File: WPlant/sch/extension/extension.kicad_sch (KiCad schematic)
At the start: 37 parts, among them J1 PROG/SWD, J2 HumSnc, J3 HumSnc, J4 HumSnc, J5 HumSnc, J6 Input, J7 Output, J8 LeakDetect, J9 Valves, Q1 FDS9926A, Q2 FDS9926A, U1 PY32F003F18P6TU, U2 74HC594, U3 4052, U4 AIP485BSA8.TB, U5 AIP485BSA8.TB, U6 AP2204R-5.0

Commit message: Extension sch update
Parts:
- U3: value 4052 -> 74HC4052
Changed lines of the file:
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@@
 			)
 		)
-		(property "Value" "4052"
+		(property "Value" "74HC4052"
 			(at 230.7941 99.06 0)
 			(effects

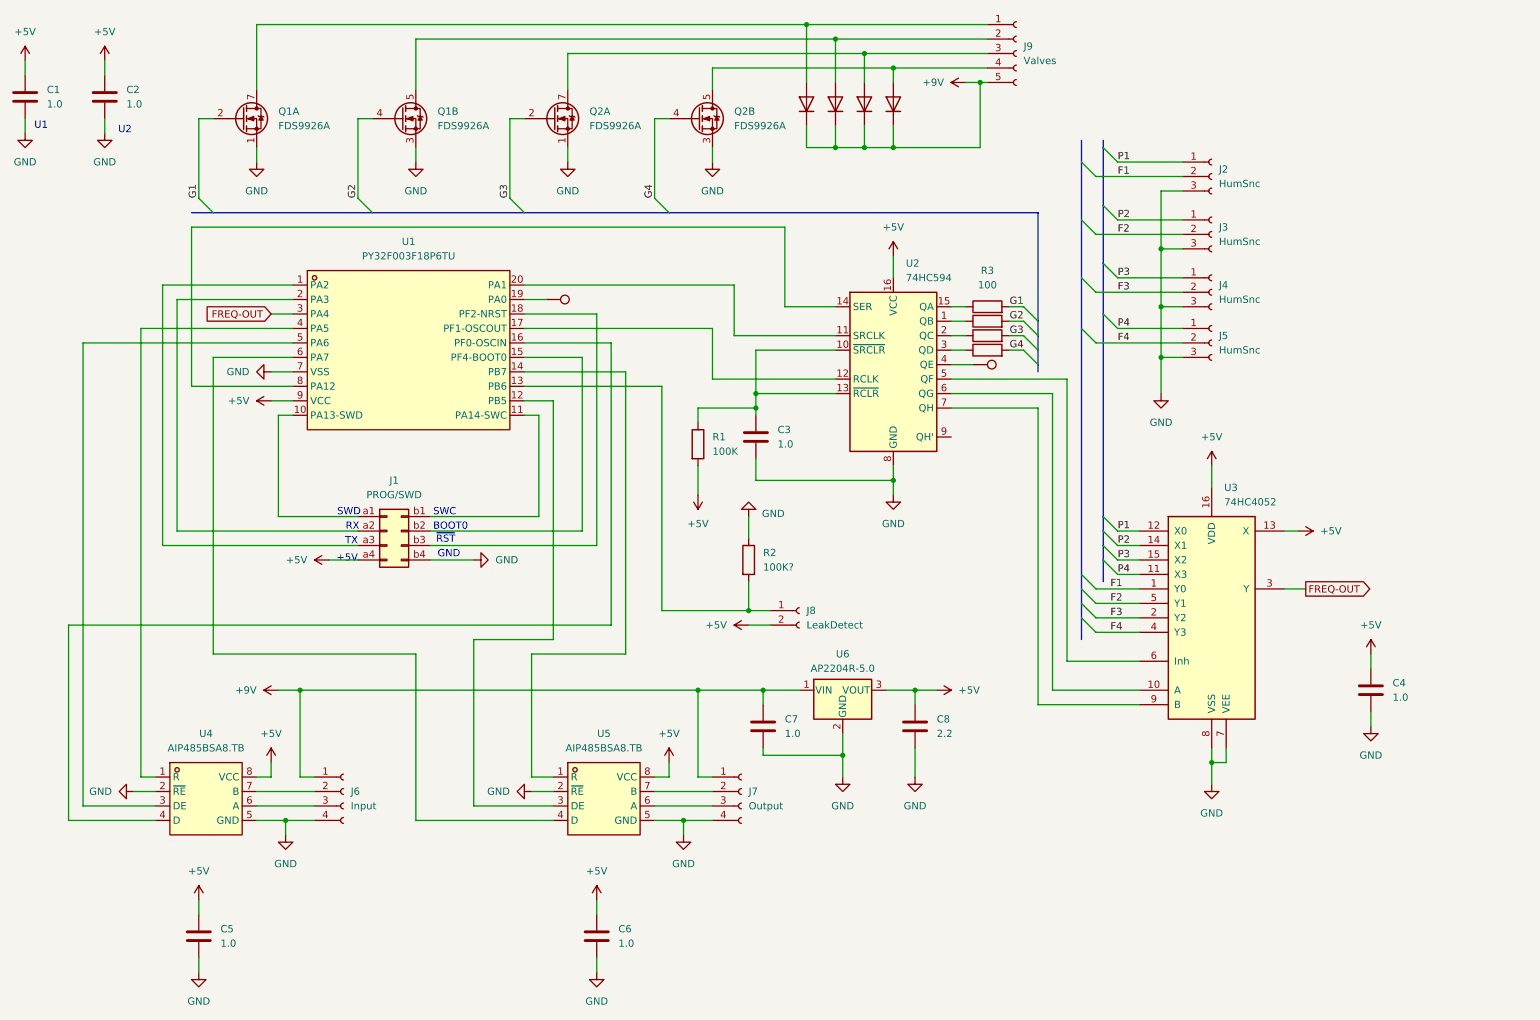
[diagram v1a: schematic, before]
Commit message: Updated Generic WP schematic
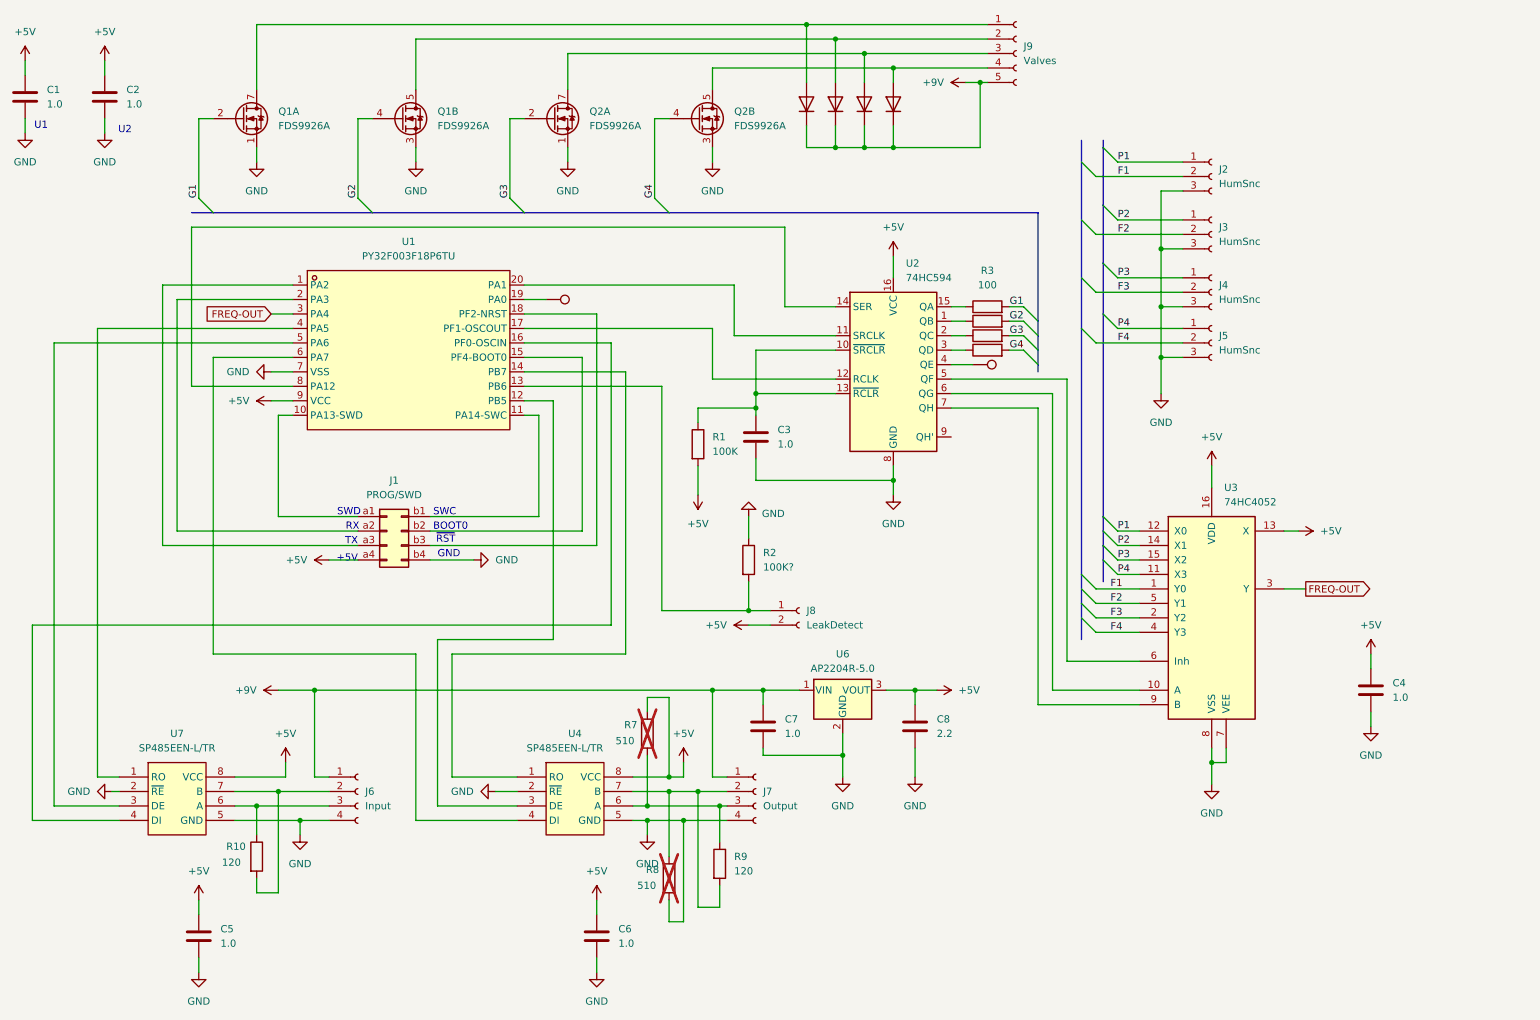
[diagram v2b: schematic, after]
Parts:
- removed U4, U5: AIP485BSA8.TB, easyeda2kicad:SOP-8_L4.9-W3.9-P1.27-LS6.0-BL, symbol EasyEDA:AIP485BSA8.TB
- added R10, R9: 120, symbol Device:R
- added R7, R8: 510, symbol Device:R
- added U4, U7: SP485EEN-L/TR, easyeda2kicad:SOIC-8_L5.0-W4.0-P1.27-LS6.0-BL, symbol EasyEDA:SP485EEN-L_TR
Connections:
- net +5V: now also R7.1, U4.8 (VCC), U7.8 (VCC)
- net GND: now also R8.2, U4.2 (~{RE}), U4.5 (GND), U7.2 (~{RE}), U7.5 (GND)
- net at J7.2 (Pin_2): now also R8.1, R9.2, U4.7 (B)
- net at J7.3 (Pin_3): now also R7.2, R9.1, U4.6 (A)
- net at U1.12 (PB5): now also U4.3 (DE)
- net at U1.14 (PB7): now also U4.1 (RO)
- net at U1.16 (PF0-OSCIN): now also U7.4 (DI)
- net at U1.4 (PA5): now also U7.1 (RO)
- net at U1.5 (PA6): now also U7.3 (DE)
- net at U1.6 (PA7): now also U4.4 (DI)
- net at J6.3 (Pin_3): now also R10.1, U7.6 (A)
- net at J6.2 (Pin_2): now also R10.2, U7.7 (B)
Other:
- moved on the sheet: J6, J7

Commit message: PCB for Extension block (of WP) ready
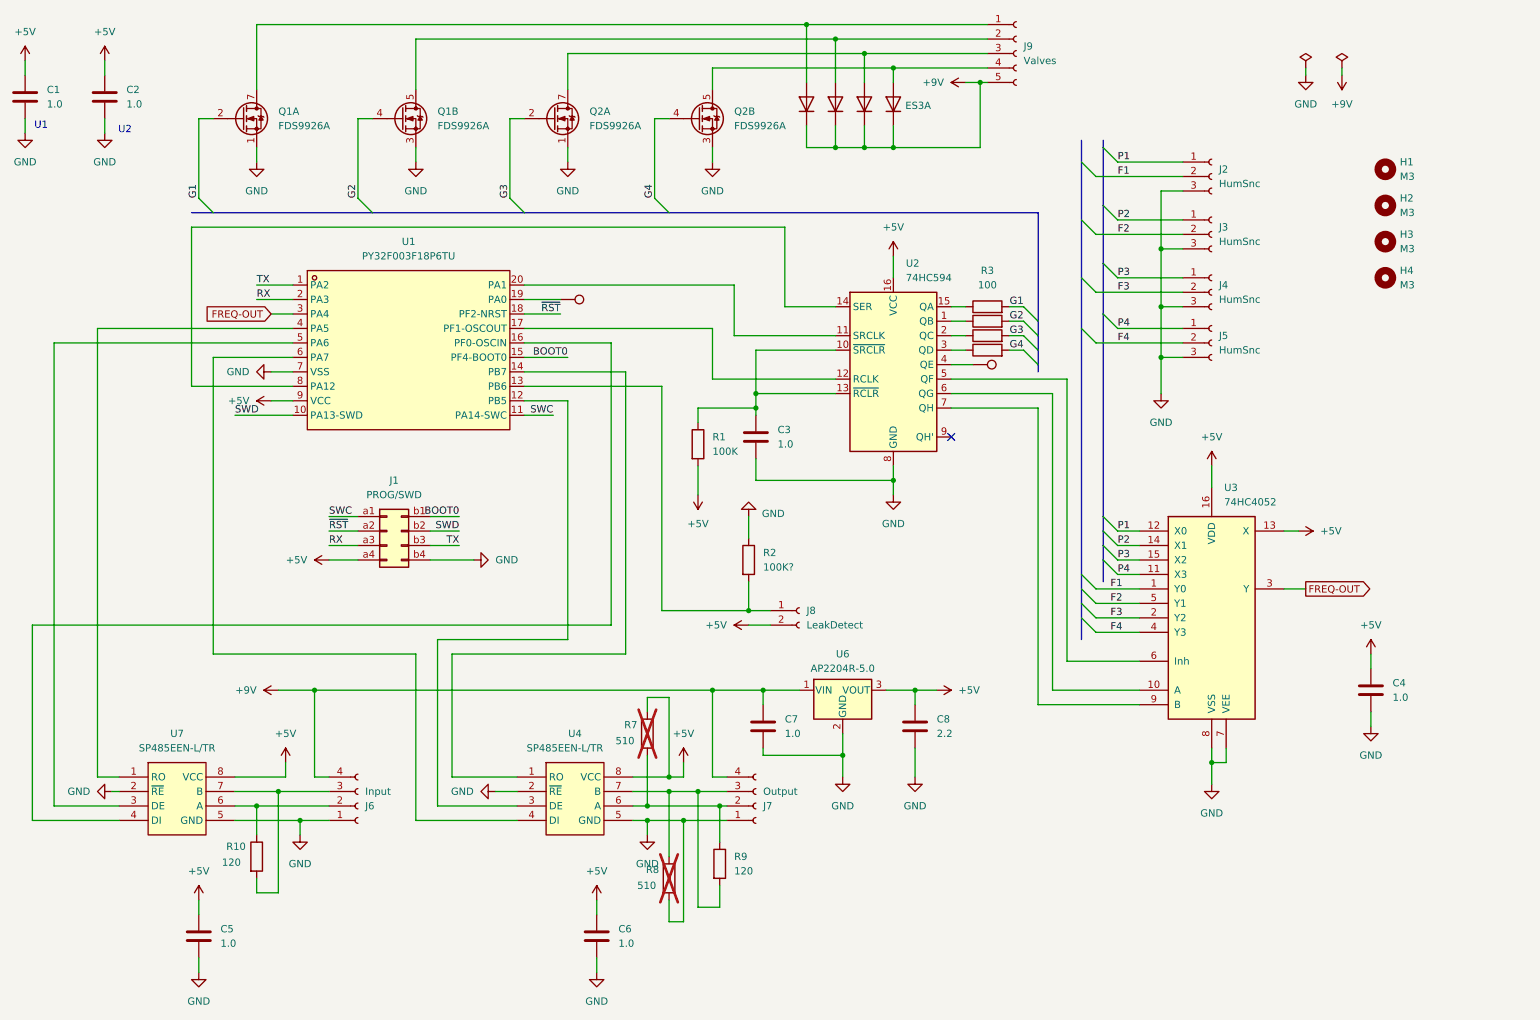
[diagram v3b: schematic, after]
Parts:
- added H1, H2, H3, H4: M3, MountingHole:MountingHole_3.2mm_M3, symbol Mechanical:MountingHole
- C1, C2, C3, C4, C5, C6, C7, C8: footprint (none) -> Capacitor_SMD:C_0603_1608Metric_Pad1.08x0.95mm_HandSolder
- D1, D2, D3, D4: value D -> ES3A; footprint (none) -> Diode_SMD:D_SMC
- J1: footprint (none) -> Connector_PinHeader_2.54mm:PinHeader_2x04_P2.54mm_Vertical
- J2, J3, J4, J5: footprint (none) -> easyeda2kicad:CONN-TH_DB301R-3.5-3P-GN-S
- J6, J7: footprint (none) -> local:CONN-TH_DB301R-3.5-4P-GN-S
- J8: footprint (none) -> Connector_JST:JST_XH_B2B-XH-A_1x02_P2.50mm_Vertical
- J9: footprint (none) -> Connector_JST:JST_XH_B5B-XH-A_1x05_P2.50mm_Vertical
- R1, R10, R2, R3, R4, R5, R6, R7, R8, R9: footprint (none) -> Resistor_SMD:R_0603_1608Metric_Pad0.98x0.95mm_HandSolder
- TP1, TP2: footprint (none) -> TestPoint:TestPoint_Pad_1.0x1.0mm
- U2: footprint (none) -> easyeda2kicad:SOIC-16_L9.9-W3.9-P1.27-LS6.0-BL
- U3: footprint (none) -> easyeda2kicad:SOP-16_L10.0-W3.9-P1.27-LS6.0-BL
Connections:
- net +9V: now also J6.4 (Pin_4), J7.4 (Pin_4); no longer J6.1 (Pin_1), J7.1 (Pin_1)
- net GND: now also J6.1 (Pin_1), J7.1 (Pin_1); no longer J6.4 (Pin_4), J7.4 (Pin_4)
- net SWC: now reaches J1.a1 (Pin_a1)
- net SWC: now also U1.11 (PA14-SWC); no longer U1.10 (PA13-SWD)
- net RX: now reaches U1.2 (PA3)
- net RX: now also J1.a3 (Pin_a3); no longer J1.a2 (Pin_a2)
- net TX: now reaches U1.1 (PA2)
- net TX: now also J1.b3 (Pin_b3); no longer J1.a3 (Pin_a3)
- net BOOT0: now reaches J1.b1 (Pin_b1)
- net BOOT0: now also U1.15 (PF4-BOOT0); no longer U1.11 (PA14-SWC)
- net SWD: now reaches J1.b2 (Pin_b2)
- net SWD: now also U1.10 (PA13-SWD); no longer U1.15 (PF4-BOOT0)
- net ~{RST}: now reaches U1.18 (PF2-NRST)
- net ~{RST}: now also J1.a2 (Pin_a2); no longer J1.b3 (Pin_b3)
- net at R8.1, R9.2, U4.7 (B): now also J7.3 (Pin_3); no longer J7.2 (Pin_2)
- net at R7.2, R9.1, U4.6 (A): now also J7.2 (Pin_2); no longer J7.3 (Pin_3)
- net at R10.1, U7.6 (A): now also J6.2 (Pin_2); no longer J6.3 (Pin_3)
- net at R10.2, U7.7 (B): now also J6.3 (Pin_3); no longer J6.2 (Pin_2)
- no-connect marks 0 -> 1
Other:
- note removed: "+5V"
- note removed: "BOOT0"
- note removed: "GND"
- note removed: "RX"
- note removed: "SWC"
- note removed: "SWD"
- note removed: "TX"
- note removed: "~{RST}"

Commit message: Update WP Extension and Generic
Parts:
- added C10: 100, Capacitor_THT:CP_Radial_D5.0mm_P2.00mm, symbol Device:C_Polarized
- added C9: NP, Capacitor_SMD:C_1206_3216Metric_Pad1.33x1.80mm_HandSolder, symbol Device:C
- added R11: 100, Resistor_SMD:R_0603_1608Metric_Pad0.98x0.95mm_HandSolder, symbol Device:R
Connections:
- net +5V: now also C9.1, R11.2; no longer U3.13 (X)
- net +9V: now also C10.1
- net GND: now also C10.2, C9.2
- new net: R11.1, U3.13 (X)

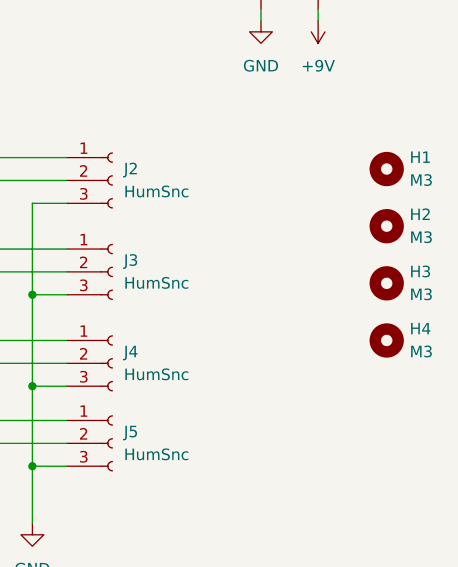
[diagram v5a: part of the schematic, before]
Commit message: Addeed places for latches on Extension board. Updated MainInt sch and pcb
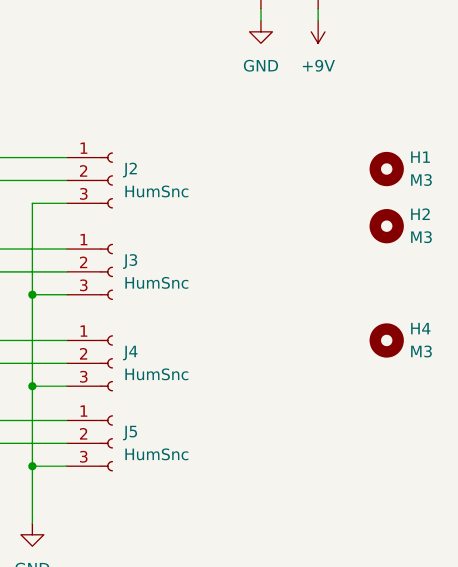
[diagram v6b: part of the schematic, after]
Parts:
- removed H3: M3, MountingHole:MountingHole_3.2mm_M3, symbol Mechanical:MountingHole
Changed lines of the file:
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@@
-	)
-	(symbol
-		(lib_id "Mechanical:MountingHole")
-		(at 259.08 53.34 0)
-		(unit 1)
-		(exclude_from_sim yes)
-		(in_bom no)
-		(on_board yes)
-		(dnp no)
-		(fields_autoplaced yes)
-		(property "Reference" "H3"
-			(at 261.62 52.0699 0)
-			(effects
-				(font
-					(size 1.27 1.27)
-				)
-				(justify left)
-			)
-		)
-		(property "Value" "M3"
-			(at 261.62 54.6099 0)
-			(effects
-				(font
-					(size 1.27 1.27)
-				)
-				(justify left)
-			)
-		)
-		(property "Footprint" "MountingHole:MountingHole_3.2mm_M3"
-			(at 259.08 53.34 0)
-			(effects
-				(font
-					(size 1.27 1.27)
-				)
-				(hide yes)
-			)
-		)
-		(property "Datasheet" "~"
-			(at 259.08 53.34 0)
-			(effects
-				(font
-					(size 1.27 1.27)
-				)
-				(hide yes)
-			)
-		)
-		(property "Description" "Mounting Hole without connection"
-			(at 259.08 53.34 0)
-			(effects
-				(font
-					(size 1.27 1.27)
-				)
-				(hide yes)
-			)
-		)
-		(instances
-			(project "extension"
-				(path "/effe5716-54fc-433b-a0c9-16665c5006c9"
-					(reference "H3")
-					(unit 1)
-				)
-			)
-		)
 	)
 	(symbol
